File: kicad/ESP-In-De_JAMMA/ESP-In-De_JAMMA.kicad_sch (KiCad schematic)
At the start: 45 parts

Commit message: Adjustments
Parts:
- removed C? (x2): 0.1uF, symbol Device:C_Small
- added C? (x2): 0.1uF, symbol Device:C_Small
- SW?: value Rotary -> PEC12R-2217F-S0024
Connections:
- net +3V3: now also C?.1, C?.1
- net GND: now also C?.2, C?.2
- no-connect marks 18 -> 22
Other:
- moved on the sheet: C?, J?, R?, RN?, SW?, U?

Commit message: Minor changes
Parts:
- added J?: CPS2 Kick Header, symbol ESP-In-De_Symbols:CPS2 Kick Header
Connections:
- net GND: now also J?.31 (Vol_GND), J?.33 (P2_GND), J?.34 (P1_GND)
- no-connect marks 22 -> 24
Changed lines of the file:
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@@
   (junction (at 24.13 158.75) (diameter 0) (color 0 0 0 0)
   )
+  (junction (at 265.43 182.88) (diameter 0) (color 0 0 0 0)
+  )
   (junction (at 128.27 227.33) (diameter 0) (color 0 0 0 0)
   )
@@
   (junction (at 321.31 162.56) (diameter 0) (color 0 0 0 0)
   )
+  (junction (at 271.78 186.69) (diameter 0) (color 0 0 0 0)
+  )
   (junction (at 406.4 175.26) (diameter 0) (color 0 0 0 0)
   )
@@
   (no_connect (at 26.67 86.36))
   (no_connect (at 68.58 86.36))
+  (no_connect (at 265.43 177.8))
+  (no_connect (at 278.13 177.8))
   (no_connect (at 354.33 170.18))
   (no_connect (at 354.33 172.72))
@@
     (stroke (width 0) (type default) (color 0 0 0 0))
   )
+  (wire (pts (xy 265.43 182.88) (xy 265.43 186.69))
+    (stroke (width 0) (type default) (color 0 0 0 0))
+  )
   (wire (pts (xy 171.45 255.27) (xy 151.13 255.27))
     (stroke (width 0) (type default) (color 0 0 0 0))
@@
     (stroke (width 0) (type default) (color 0 0 0 0))
   )
+  (wire (pts (xy 265.43 180.34) (xy 265.43 182.88))
+    (stroke (width 0) (type default) (color 0 0 0 0))
+  )
   (wire (pts (xy 334.01 119.38) (xy 321.31 119.38))
     (stroke (width 0) (type default) (color 0 0 0 0))
@@
     (stroke (width 0) (type default) (color 0 0 0 0))
   )
+  (wire (pts (xy 278.13 186.69) (xy 271.78 186.69))
+    (stroke (width 0) (type default) (color 0 0 0 0))
+  )
   (wire (pts (xy 104.14 110.49) (xy 133.35 110.49))
     (stroke (width 0) (type default) (color 0 0 0 0))
@@
     (stroke (width 0) (type default) (color 0 0 0 0))
   )
+  (wire (pts (xy 265.43 186.69) (xy 271.78 186.69))
+    (stroke (width 0) (type default) (color 0 0 0 0))
+  )
   (polyline (pts (xy 182.88 264.16) (xy 87.63 264.16))
     (stroke (width 0) (type default) (color 0 0 0 0))
@@
     (stroke (width 0) (type default) (color 0 0 0 0))
   )
+  (wire (pts (xy 278.13 182.88) (xy 278.13 186.69))
+    (stroke (width 0) (type default) (color 0 0 0 0))
+  )
   (wire (pts (xy 138.43 255.27) (xy 138.43 247.65))
     (stroke (width 0) (type default) (color 0 0 0 0))
@@
     (pin "2")
   )
+  (symbol (lib_id "power:GND") (at 271.78 186.69 0) (unit 1)
+    (in_bom yes) (on_board yes) (fields_autoplaced)
+    (property "Reference" "#PWR?" (id 0) (at 271.78 193.04 0)
+      (effects (font (size 1.27 1.27)) hide)
+    )
+    (property "Value" "GND" (id 1) (at 271.78 191.2525 0))
+    (property "Footprint" "" (id 2) (at 271.78 186.69 0)
+      (effects (font (size 1.27 1.27)) hide)
+    )
+    (property "Datasheet" "" (id 3) (at 271.78 186.69 0)
+      (effects (font (size 1.27 1.27)) hide)
+    )
+    (pin "1")
+  )
   (symbol (lib_id "td_symbols:JAMMA_Edge") (at 29.21 151.13 0) (unit 1)
     (in_bom yes) (on_board yes) (fields_autoplaced)
@@
     (pin "S2")
   )
+  (symbol (lib_id "ESP-In-De_Symbols:CPS2 Kick Header") (at 271.78 162.56 0) (unit 1)
+    (in_bom yes) (on_board yes) (fields_autoplaced)
+    (property "Reference" "J?" (id 0) (at 271.78 137.0035 0))
+    (property "Value" "CPS2 Kick Header" (id 1) (at 271.78 139.7786 0))
+    (property "Footprint" "" (id 2) (at 270.51 162.56 0)
+      (effects (font (size 1.27 1.27)) hide)
+    )
+    (property "Datasheet" "https://www.digikey.com/en/products/detail/hirose-electric-co-ltd/DF1BZ-34DP-2-5DSA/1033186?s=N4IgjCBcoBw1oDGUBmBDANgZwKYBoQB7KAbXAE4AGAVgGZqQBdAgBwBcoQBlNgJwEsAdgHMQAXwIBaAEwIQySHwCu%2BIqRANGYiSFmQyAEQBiYAEJMxQA" (id 3) (at 271.78 134.62 0)
+      (effects (font (size 1.27 1.27)) hide)
+    )
+    (pin "1")
+    (pin "10")
+    (pin "11")
+    (pin "12")
+    (pin "13")
+    (pin "14")
+    (pin "15")
+    (pin "16")
+    (pin "17")
+    (pin "18")
+    (pin "19")
+    (pin "2")
+    (pin "20")
+    (pin "21")
+    (pin "22")
+    (pin "23")
+    (pin "24")
+    (pin "25")
+    (pin "26")
+    (pin "27")
+    (pin "28")
+    (pin "29")
+    (pin "3")
+    (pin "30")
+    (pin "31")
+    (pin "32")
+    (pin "33")
+    (pin "34")
+    (pin "4")
+    (pin "5")
+    (pin "6")
+    (pin "7")
+    (pin "8")
+    (pin "9")
+  )
   (symbol (lib_id "power:GND") (at 17.78 22.86 0) (unit 1)
     (in_bom yes) (on_board yes) (fields_autoplaced)
@@
       (reference "#PWR?") (unit 1) (value "GND") (footprint "")
     )
+    (path "/2e79def6-5551-41cf-89c3-16de92f773ee"
+      (reference "#PWR?") (unit 1) (value "GND") (footprint "")
+    )
     (path "/3e5f16ee-2d28-4577-abf5-95349ed5dcd9"
       (reference "#PWR?") (unit 1) (value "+5V") (footprint "")
@@
       (reference "J?") (unit 1) (value "JAMMA to Game Board") (footprint "td-symbols:JAMMA")
     )
+    (path "/b1ab5498-dd39-4c30-a9bf-3b9cb5010d83"
+      (reference "J?") (unit 1) (value "CPS2 Kick Header") (footprint "")
+    )
     (path "/22a07587-6573-4419-bc39-976cee5ef450"

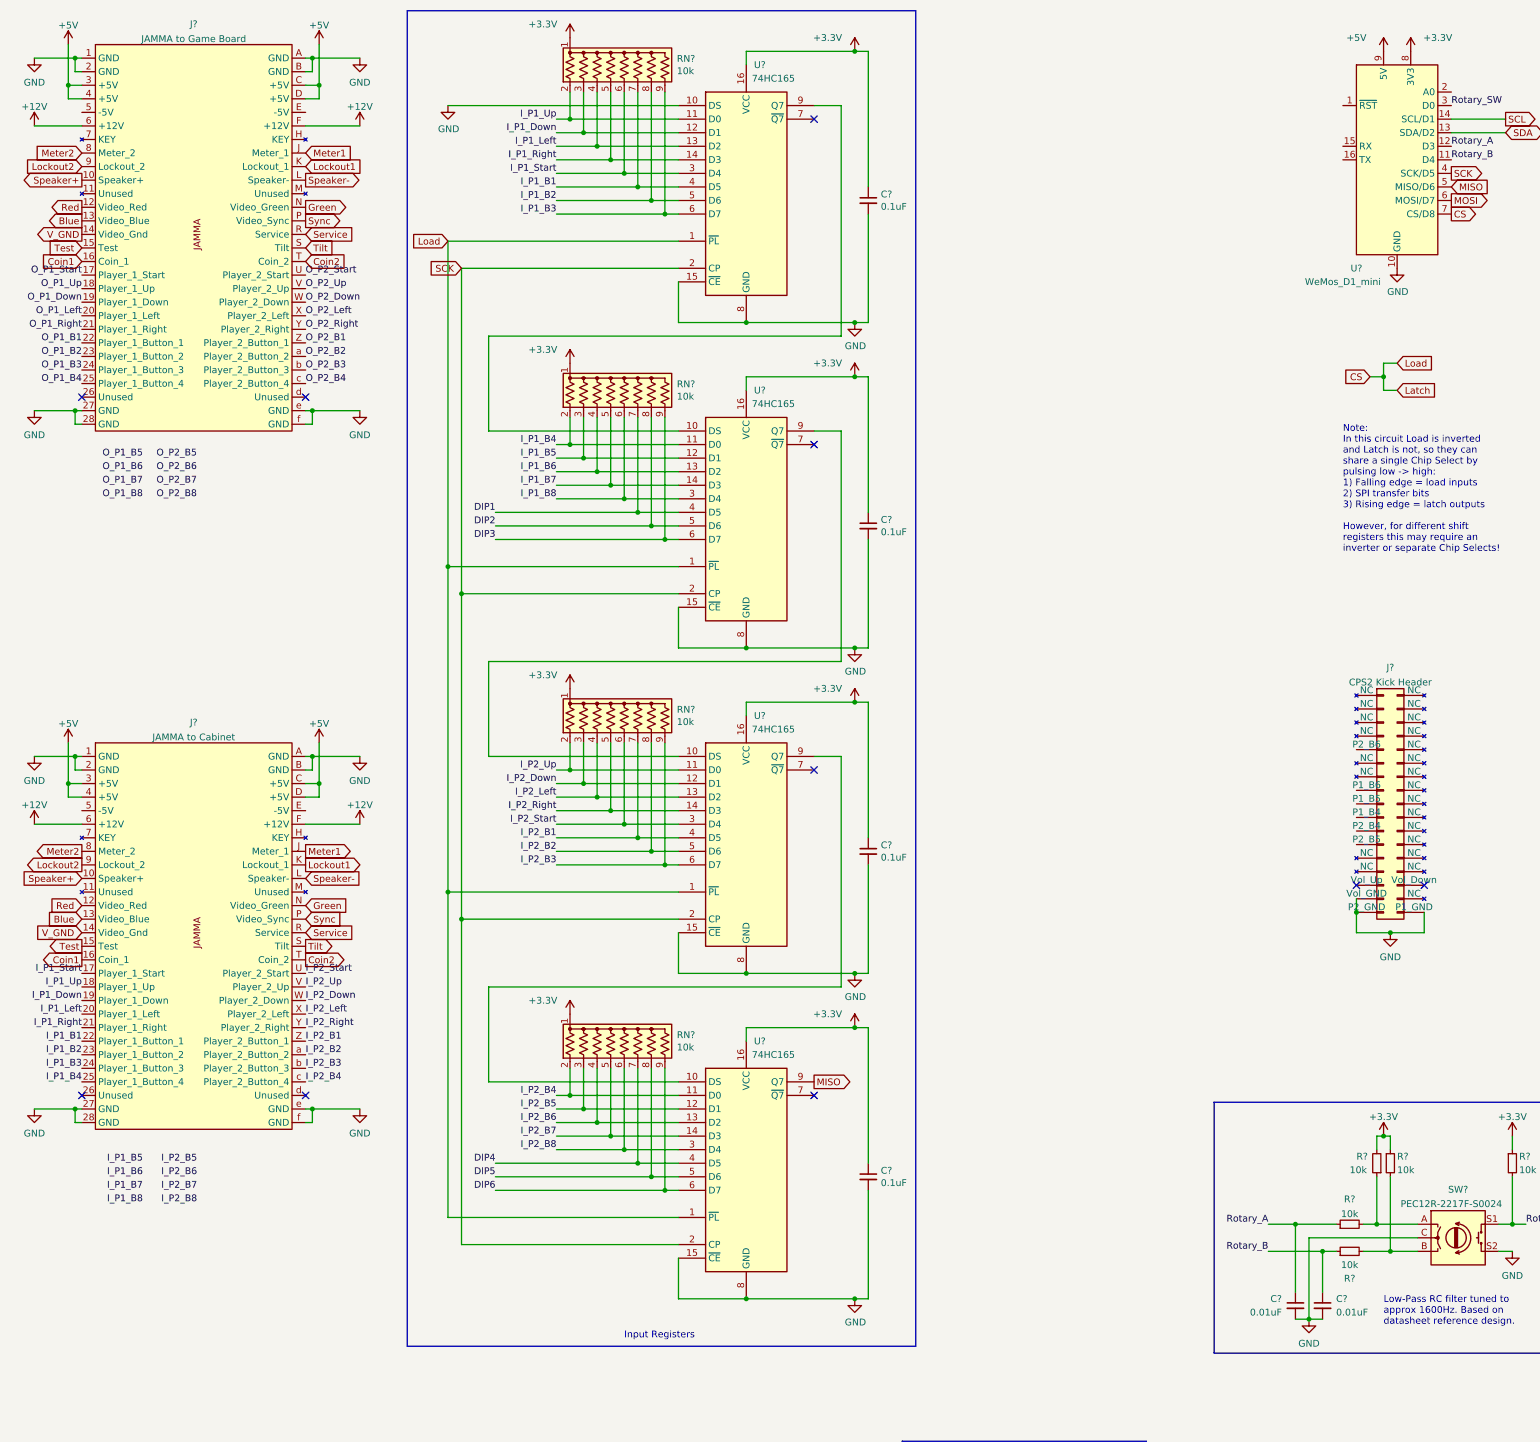
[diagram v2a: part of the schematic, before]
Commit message: README updates, old desc, sch update Kick button labels, update JAMMAA symbol
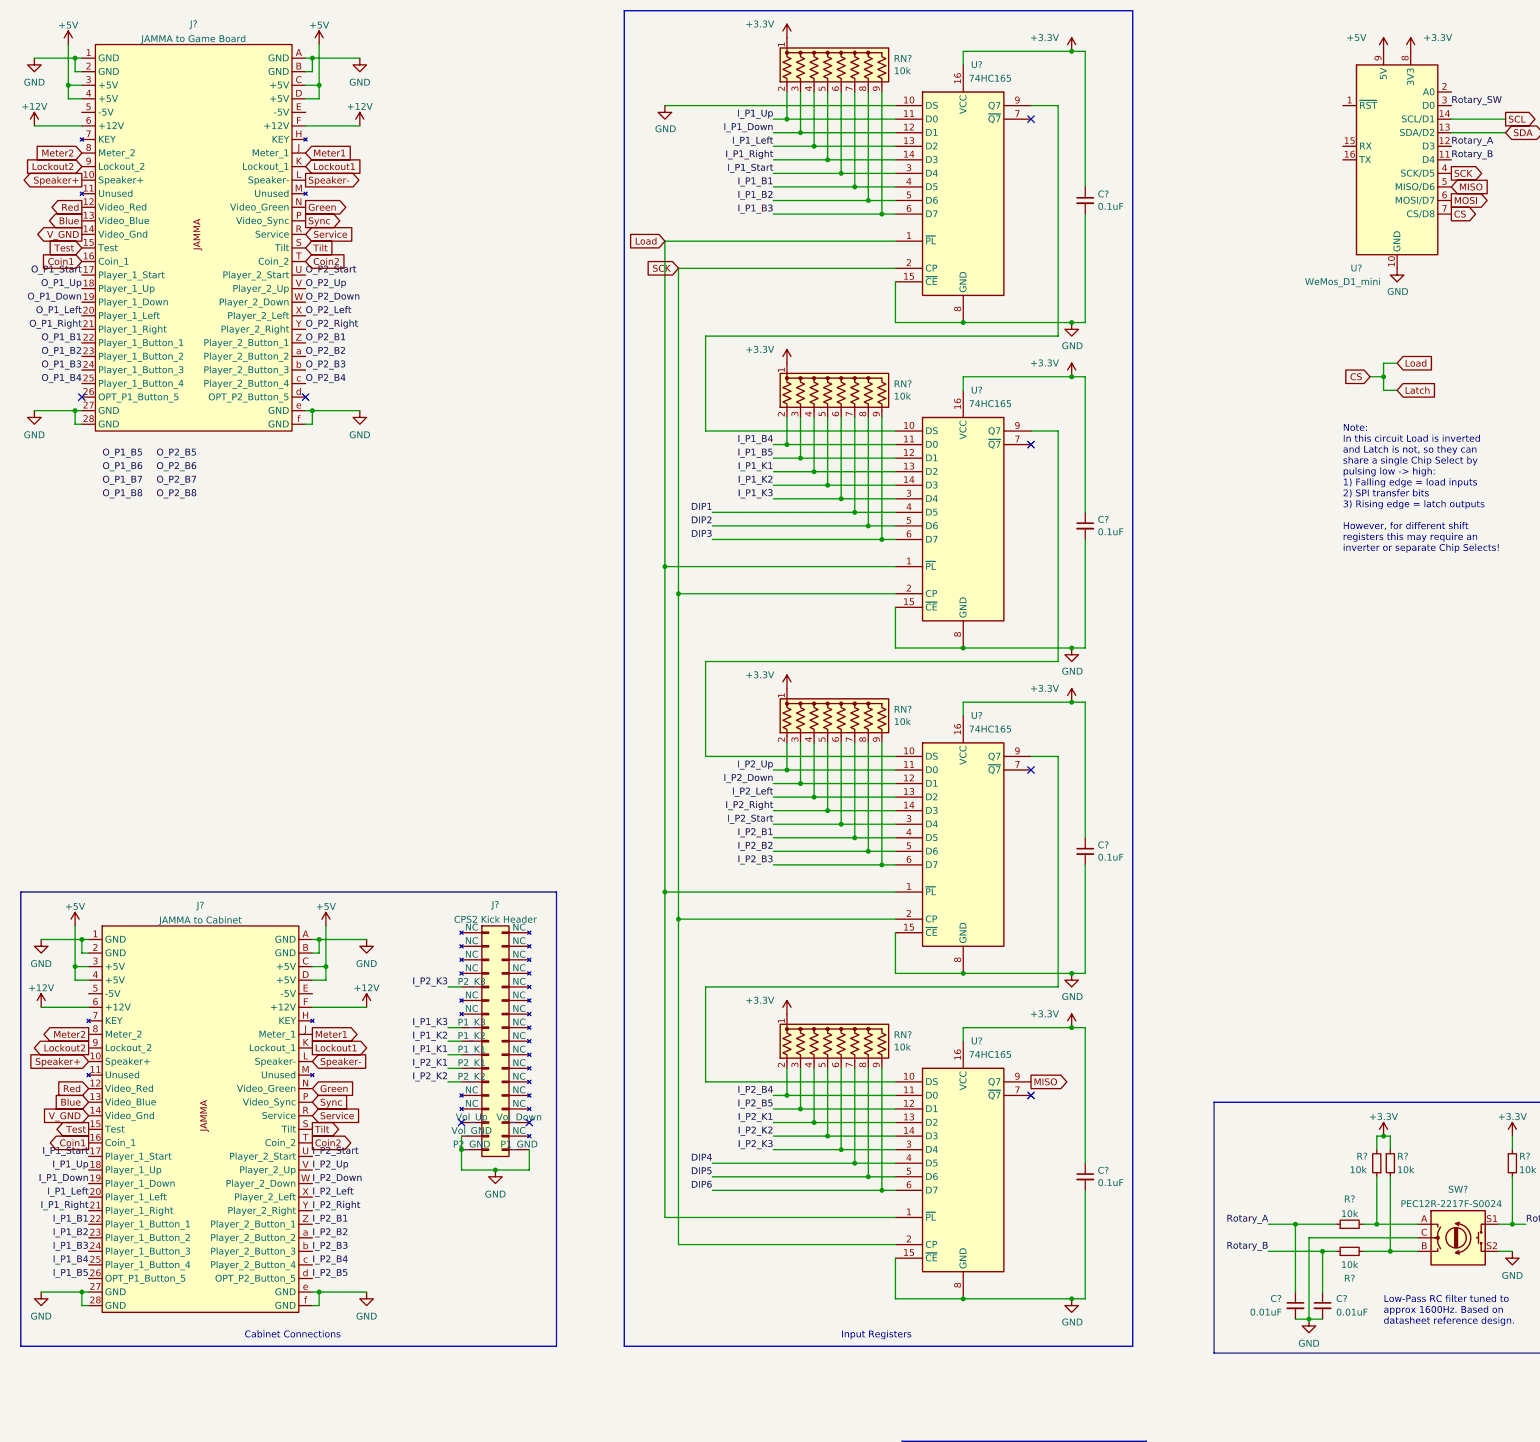
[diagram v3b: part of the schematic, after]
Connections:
- net I_P1_B6 is gone; now on net I_P1_K1: RN?.4 (R3), U?.13 (D2)
- net I_P1_B7 is gone; now on net I_P1_K2: RN?.5 (R4), U?.14 (D3)
- net I_P1_B8 is gone; now on net I_P1_K3: RN?.6 (R5), U?.3 (D4)
- net I_P2_B6 is gone; now on net I_P2_K1: RN?.4 (R3), U?.13 (D2)
- net I_P2_B7 is gone; now on net I_P2_K2: RN?.5 (R4), U?.14 (D3)
- net I_P2_B8 is gone; now on net I_P2_K3: RN?.6 (R5), U?.3 (D4)
- net I_P1_B5: now also J?.26 (OPT_P1_Button_5)
- net I_P2_B5: now also J?.d (OPT_P2_Button_5)
- net I_P1_K3: now reaches J?.15 (P1_K3)
- net I_P1_K2: now reaches J?.17 (P1_K2)
- net I_P1_K1: now reaches J?.19 (P1_K1)
- net I_P2_K1: now reaches J?.21 (P2_K1)
- net I_P2_K2: now reaches J?.23 (P2_K2)
- net I_P2_K3: now reaches J?.9 (P2_K3)
- no-connect marks 24 -> 22
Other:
- note added: "Cabinet Connections"
- moved on the sheet: C?, J?, RN?, U?

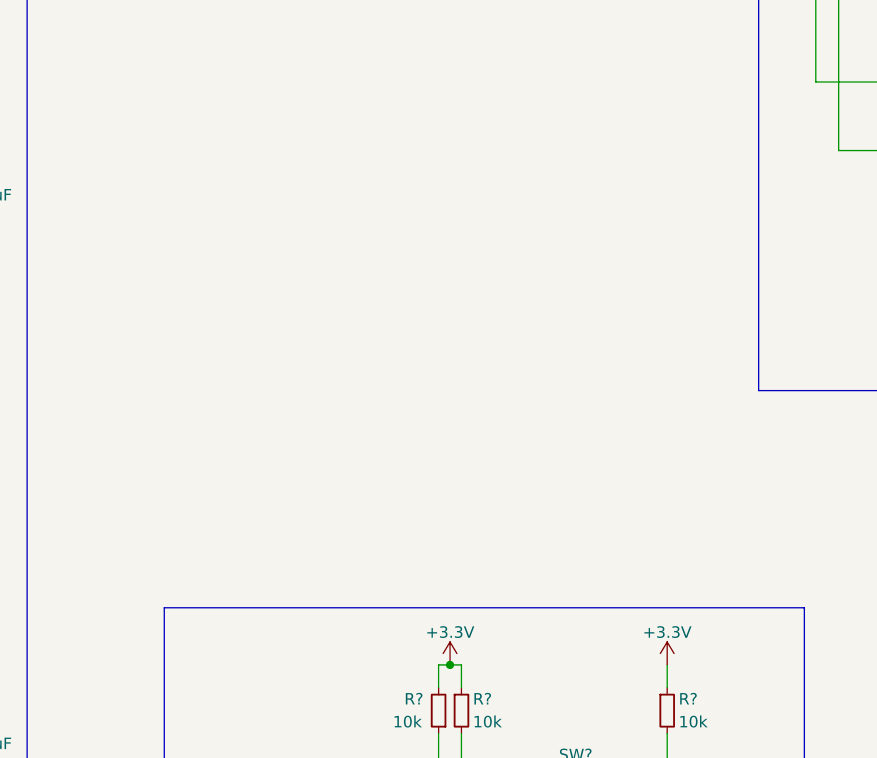
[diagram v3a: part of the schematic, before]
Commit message: Readme updates, added Readme for Data Emulator, added symbol, updated schematic with sync circuit
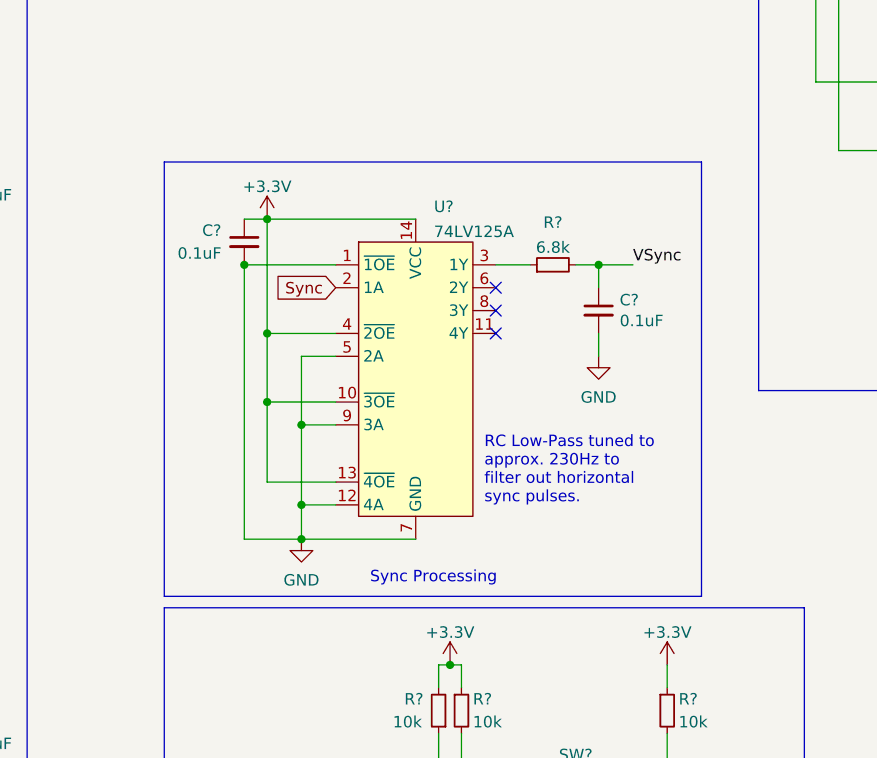
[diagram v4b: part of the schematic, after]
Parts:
- added C? (x2): 0.1uF, symbol Device:C_Small
- added R?: 6.8k, symbol Device:R_Small
- added U?: 74LV125A, Package_DIP:DIP-14_W7.62mm, symbol ESP-In-De_Symbols:74LV125A
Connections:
- net +3V3: now also C?.1, U?.10 (~{3OE}), U?.13 (~{4OE}), U?.14 (VCC), U?.4 (~{2OE})
- net GND: now also C?.2, C?.2, U?.1 (~{1OE}), U?.12 (4A), U?.5 (2A), U?.7 (GND), U?.9 (3A)
- net Sync: now also U?.2 (1A)
- new net: R?.1, U?.3 (1Y)
- new net VSync: C?.1, R?.2
- no-connect marks 22 -> 25
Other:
- note added: "RC Low-Pass tuned to approx. 230Hz to filter out horizontal sync pulses."
- note added: "Sync Processing"
